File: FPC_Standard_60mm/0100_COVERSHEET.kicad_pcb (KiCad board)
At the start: 2 copper layers, 60 x 7.5 mm, 1 part, among them J101 734150991

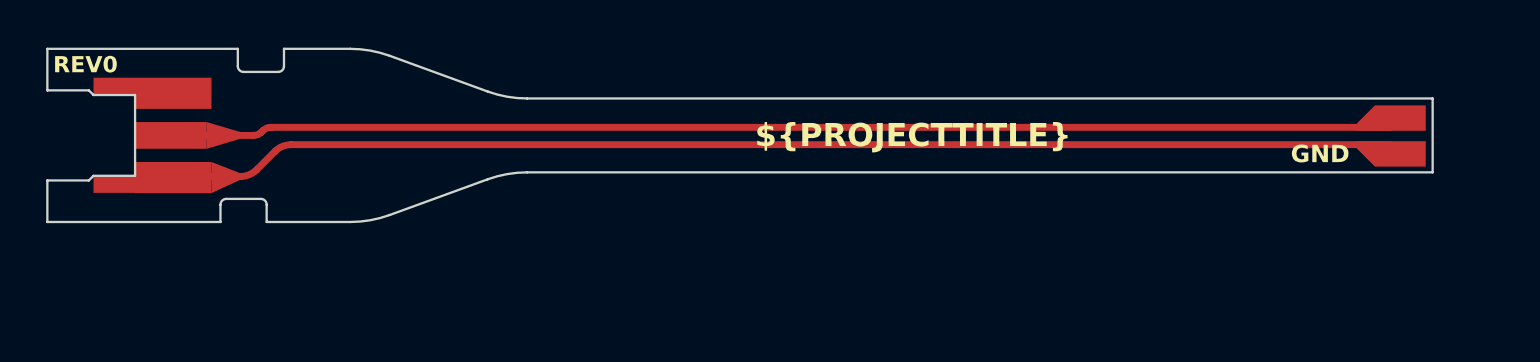
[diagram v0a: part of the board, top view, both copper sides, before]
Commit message: Renamed folder to keep naming consistency
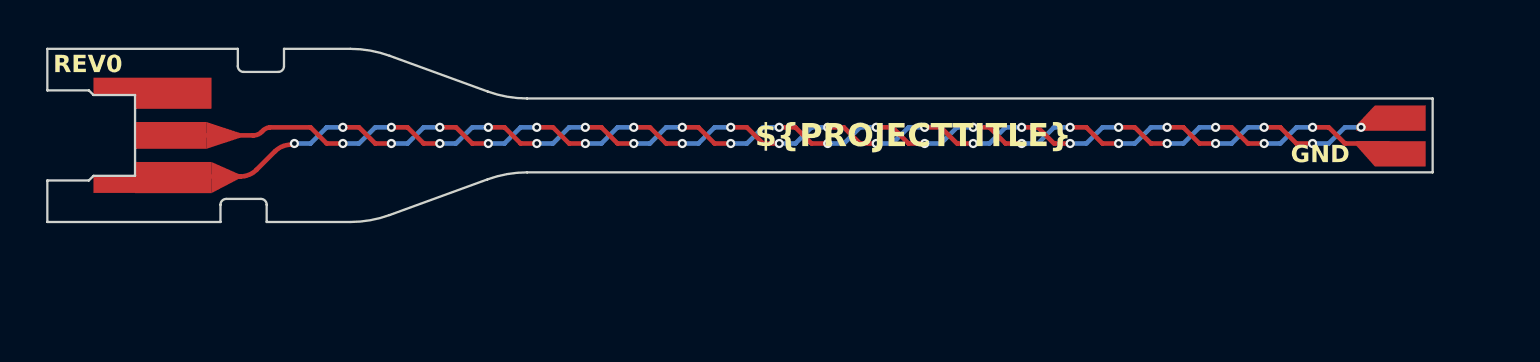
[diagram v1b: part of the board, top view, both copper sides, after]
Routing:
- net /GND: track 55.5 -> 60.6 mm, vias 0 -> 22
- net /SIGNAL: track 54.0 -> 58.0 mm, vias 0 -> 22
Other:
- board text added: "0.20"
- board text added: "0.20 mm / 0.20 mm"
- board text added: "0.35"
- board text added: "22 crossings of 0.2 mm traces -> A = 0.88 mm^2 d = 0.025 mm K = 3.3 C = K*E0*A/D = 3.3 * E0 * (0.88mm^2 / 0.025mm) = 1.03 pF"
- board text removed: "0.30"
- board text removed: "0.30 mm / 0.20 mm"
- board text removed: "0.5"

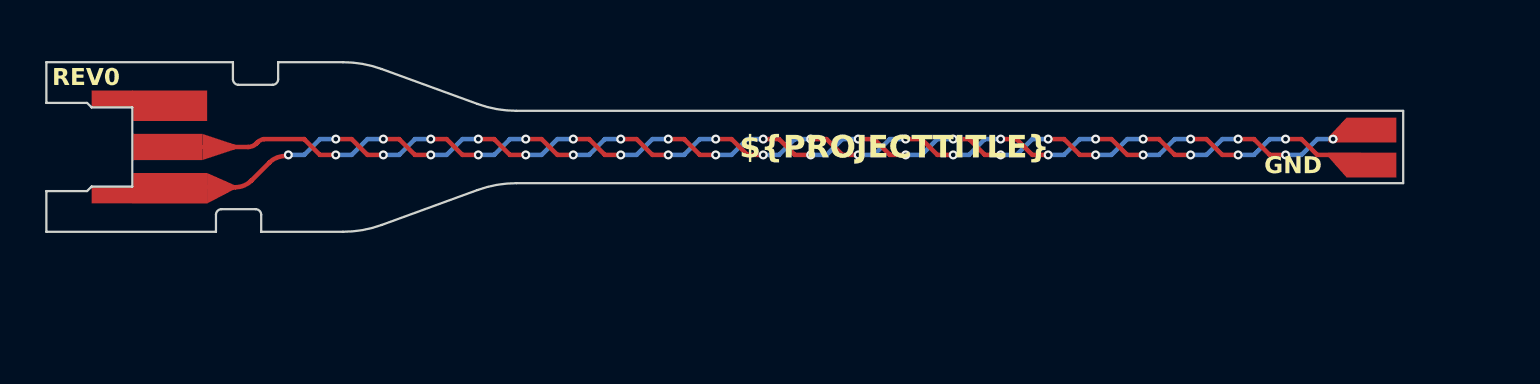
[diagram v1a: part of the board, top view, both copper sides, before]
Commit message: Changed design of the standard tip so that it will not collide with the MMCX oring. This change must be ported to the IC and 0603 probes
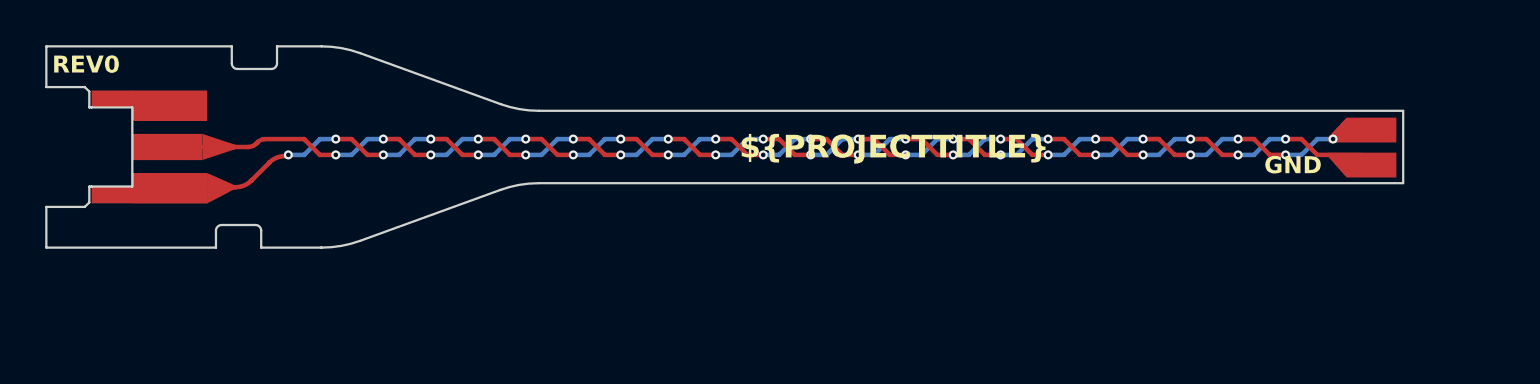
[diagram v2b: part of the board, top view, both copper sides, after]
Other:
- board size 60 x 7.5 mm -> 60 x 8.9 mm
